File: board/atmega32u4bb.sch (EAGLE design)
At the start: 18 parts, among them X3 16MHz

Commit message: V1 board design
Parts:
- removed BOOT: EVQQ2, adaprog:EVQQ2
- removed ISP6: PINHD-2X3, adaprog:PINHD-2X3
- removed L1: 500mA, adafruit:PTCFUSE-1206
- removed R4: 10K, adafruit:R-US_R0805
- removed SJ1: HWB, jumper:SJ
- removed U$5: USB_PADS, glowboard:USB_PADS
- removed X3: 16MHz, adaprog:XTALNX5032
- added Q1: 16 MHz, glowboard:ABMM2
- added S1: Normally open, glowboard:KMR211G
- added U$2: MINI_USB, glowboard:MINI_USB
- added U$4: ICSP, glowboard:ICSP
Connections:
- removed net HWB: R4.1, SJ1.1, U$1.(#HWB)PE2
- removed net N$1: L1.1, U$5.VBUS
- net GND: now also S1.P, S1.P1, U$1.(#HWB)PE2, U$2.GND, U$4.GND; no longer BOOT.S, BOOT.S1, ISP6.6, SJ1.2, U$5.GND
- net MISO: now also U$4.MISO; no longer ISP6.1
- net MOSI: now also U$4.MOSI; no longer ISP6.4
- net N$2: now also U$2.D+; no longer U$5.D+
- net N$5: now also U$2.D-; no longer U$5.D-
- net N$8: now also Q1.2; no longer X3.P$2
- net N$9: now also Q1.1; no longer X3.P$1
- net RST: now also S1.S, S1.S1, U$4.RST; no longer BOOT.P, BOOT.P1, ISP6.5
- net SCK: now also U$4.SCK; no longer ISP6.3
- net VCC: now also U$1.AREF, U$2.VBUS, U$4.VCC; no longer ISP6.2, L1.2, R4.2

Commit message: Fix some errors
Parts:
- removed C5: 10uF, adafruit:CPOL-USA/3216-18R
- added C8: 0.1uF, adafruit:C-USC0805K
- added U$5: EXPANSION_HEADER, glowboard:EXPANSION_HEADER
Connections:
- new net N$1: U$1.(ADC0)PF0, U$5.1
- new net N$6: U$1.(ADC6/TDO)PF6, U$5.2
- new net N$7: U$1.(ADC7/TDI)PF7, U$5.3
- net GND: now also C8.2; no longer C5.-
- net VCC: now also C8.1; no longer C5.+

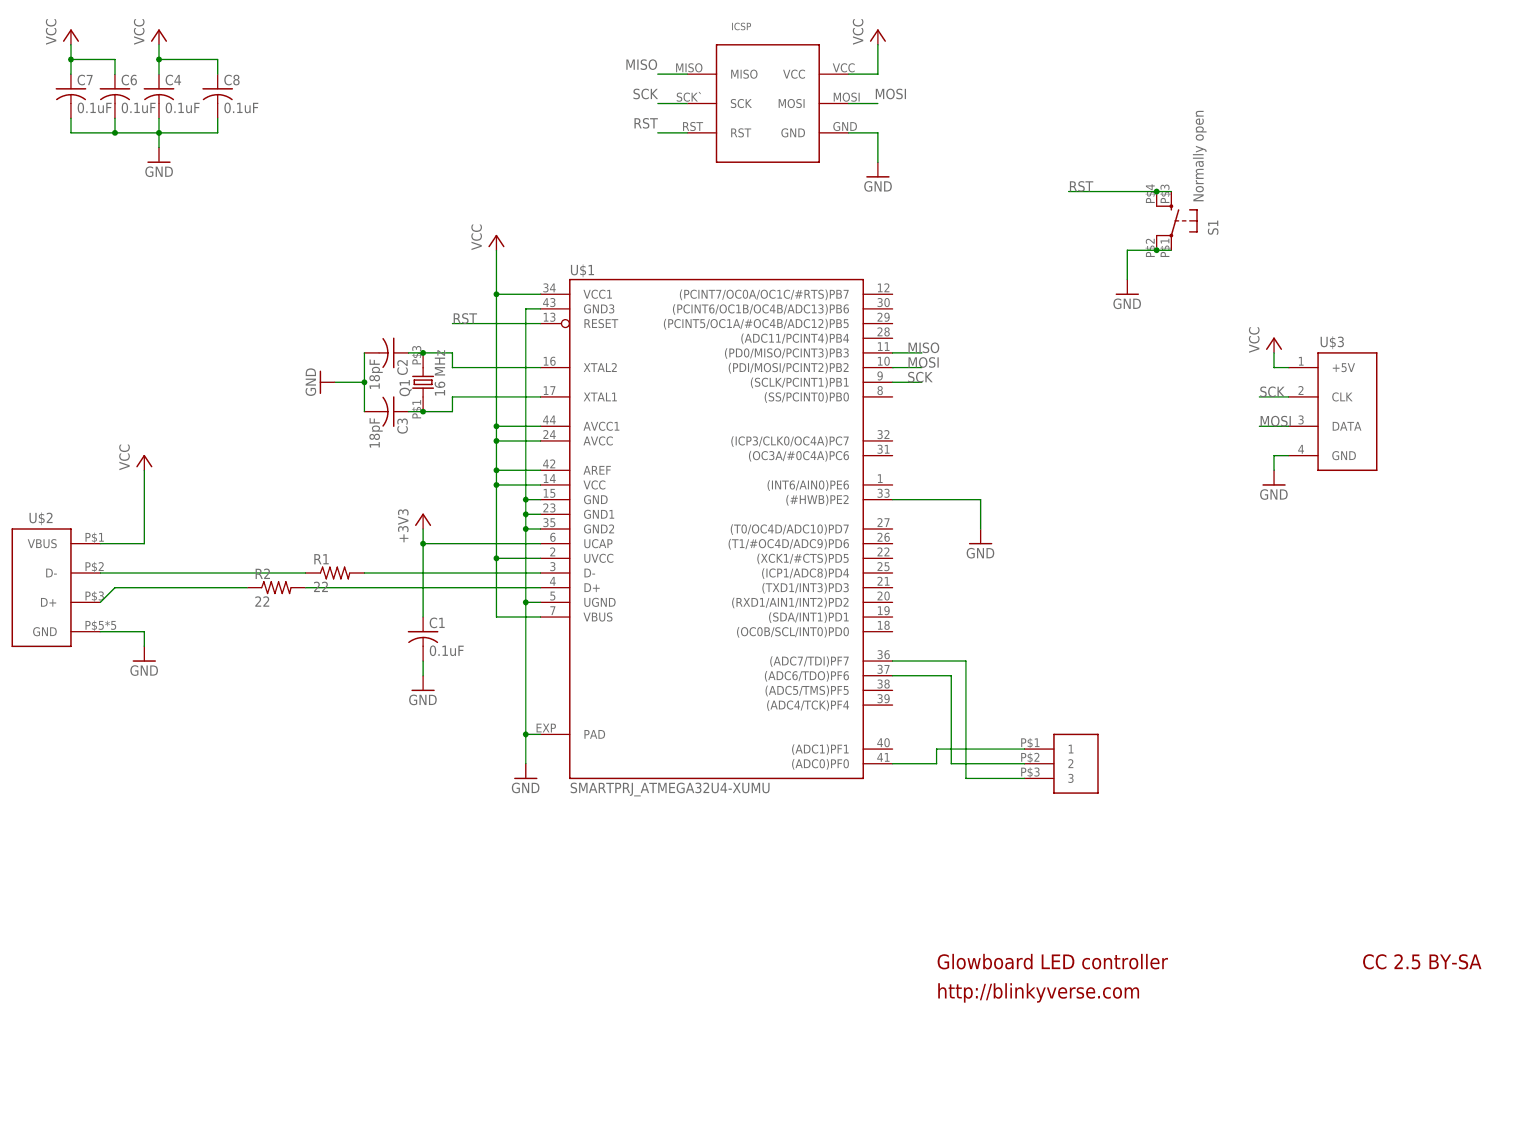
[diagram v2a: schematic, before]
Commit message: Passes DRC, add expansion header, move switch to non-reset pin.
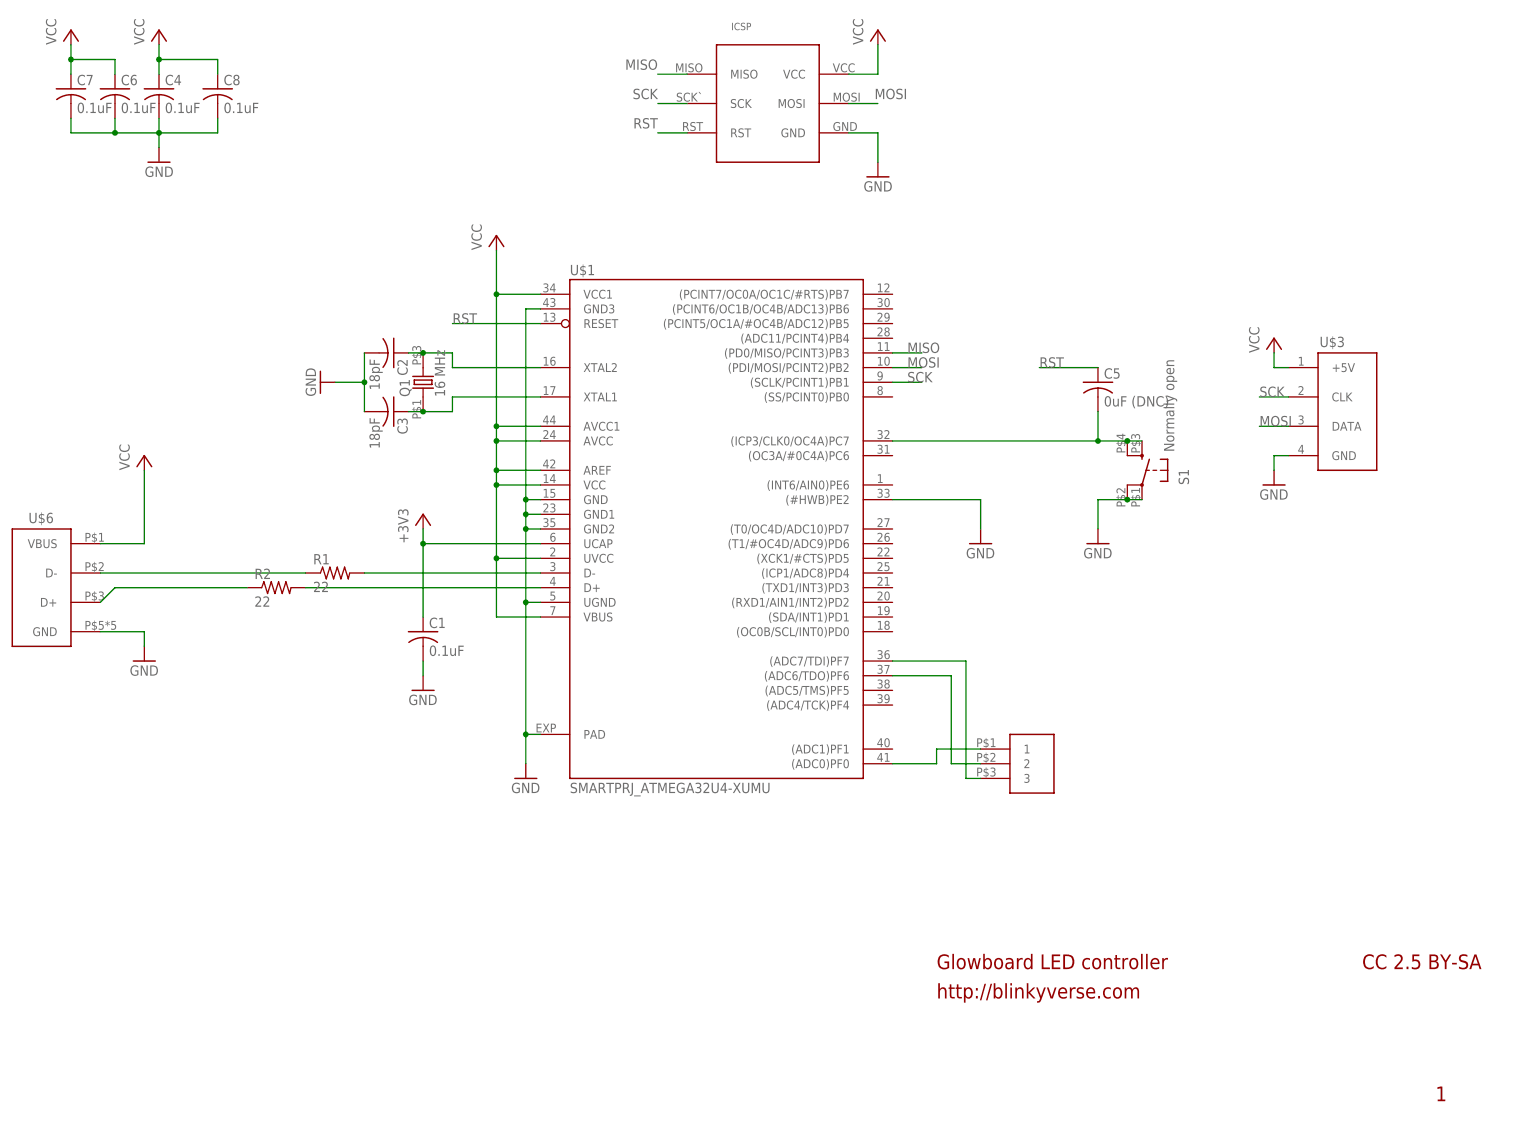
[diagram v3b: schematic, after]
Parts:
- removed U$2: MINI_USB, glowboard:MINI_USB
- added C5: 0uF (DNC), adafruit:C-USC0805K
- added U$6: GLOWBOARD_MINI_USB, blinkyboard:GLOWBOARD_MINI_USB
- U$5: value EXPANSION_HEADER -> GLOWBOARD_EXPANSION_HEADER; device glowboard:EXPANSION_HEADER -> blinkyboard:GLOWBOARD_EXPANSION_HEADER
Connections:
- new net N$10: C5.2, S1.S, S1.S1, U$1.(ICP3/CLK0/OC4A)PC7
- net GND: now also U$6.GND; no longer U$2.GND
- net N$2: now also U$6.D+; no longer U$2.D+
- net N$5: now also U$6.D-; no longer U$2.D-
- net RST: now also C5.1; no longer S1.S, S1.S1
- net VCC: now also U$6.VBUS; no longer U$2.VBUS
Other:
- note added: "1"
- moved on the sheet: S1

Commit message: Board updated! Looks ok.
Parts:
- S1: device glowboard:KMR211G -> blinkyboard:GLOWBOARD_KMR211G
- U$1: value SMARTPRJ_ATMEGA32U4-XUMU -> ARDUINO_LEONARDO-REV3B_SMARTPRJ_ATMEGA32U4-XUMU; device Arduino_Leonardo-REV3b:SMARTPRJ_ATMEGA32U4-XUMU -> blinkyboard:ARDUINO_LEONARDO-REV3B_SMARTPRJ_ATMEGA32U4-XUMU
- U$3: value PAD_CONNECTION -> GLOWBOARD_PAD_CONNECTION; device glowboard:PAD_CONNECTION -> blinkyboard:GLOWBOARD_PAD_CONNECTION
- U$4: value ICSP -> GLOWBOARD_ICSP; device glowboard:ICSP -> blinkyboard:GLOWBOARD_ICSP
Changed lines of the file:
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@@
 <part name="P+1" library="supply1" deviceset="VCC" device=""/>
 <part name="FRAME1" library="frames" deviceset="FRAME_A_L" device=""/>
-<part name="U$3" library="glowboard" deviceset="PAD_CONNECTION" device=""/>
+<part name="U$3" library="blinkyboard" deviceset="GLOWBOARD_PAD_CONNECTION" device=""/>
 <part name="P+5" library="supply1" deviceset="VCC" device=""/>
 <part name="GND5" library="supply1" deviceset="GND" device=""/>
-<part name="U$1" library="Arduino_Leonardo-REV3b" deviceset="SMARTPRJ_ATMEGA32U4-XU" device="MU"/>
+<part name="U$1" library="blinkyboard" deviceset="ARDUINO_LEONARDO-REV3B_SMARTPRJ_ATMEGA32U4-XU" device="MU"/>
 <part name="GND8" library="supply1" deviceset="GND" device=""/>
 <part name="P+6" library="supply1" deviceset="VCC" device=""/>
 <part name="P+7" library="supply1" deviceset="VCC" device=""/>
 <part name="P+8" library="supply1" deviceset="VCC" device=""/>
-<part name="S1" library="glowboard" deviceset="KMR211G" device="" value="Normally open"/>
+<part name="S1" library="blinkyboard" deviceset="GLOWBOARD_KMR211G" device="" value="Normally open"/>
 <part name="Q1" library="glowboard" deviceset="ABMM2" device="" value="16 MHz"/>
-<part name="U$4" library="glowboard" deviceset="ICSP" device=""/>
+<part name="U$4" library="blinkyboard" deviceset="GLOWBOARD_ICSP" device=""/>
 <part name="P+2" library="supply1" deviceset="VCC" device=""/>
 <part name="GND2" library="supply1" deviceset="GND" device=""/>
